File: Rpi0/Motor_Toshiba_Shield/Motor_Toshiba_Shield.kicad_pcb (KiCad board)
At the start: 2 copper layers, 29.8 x 64.8 mm, 34 parts, among them J1 Screw_Terminal_01x02, J10 Conn_01x04_Female, J11 Conn_01x04_Female, J2 Conn_02x01, J3 Screw_Terminal_01x02, J4 Screw_Terminal_01x02, J5 Screw_Terminal_01x02, J6 Screw_Terminal_01x02, J7 Conn_02x01, J8 Conn_01x04_Female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

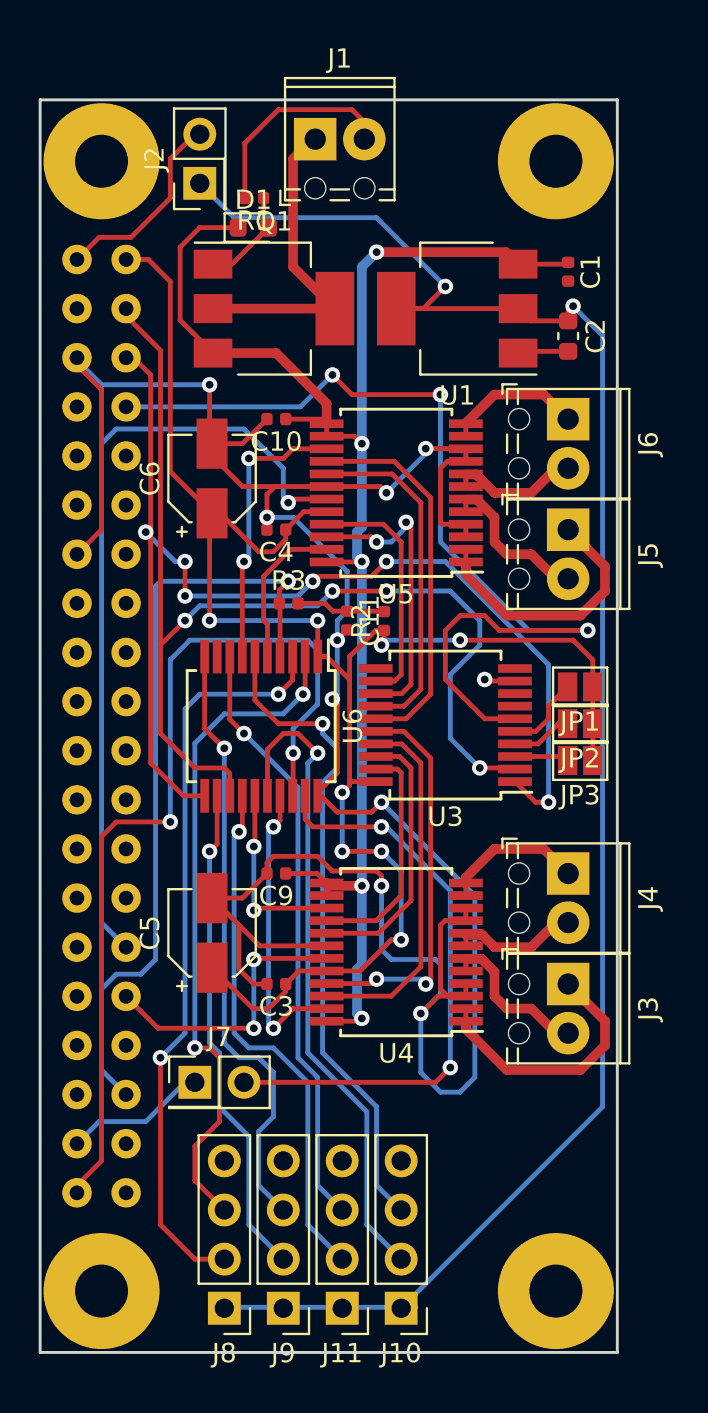
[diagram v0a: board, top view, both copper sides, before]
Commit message: Fixed rpi0 connector
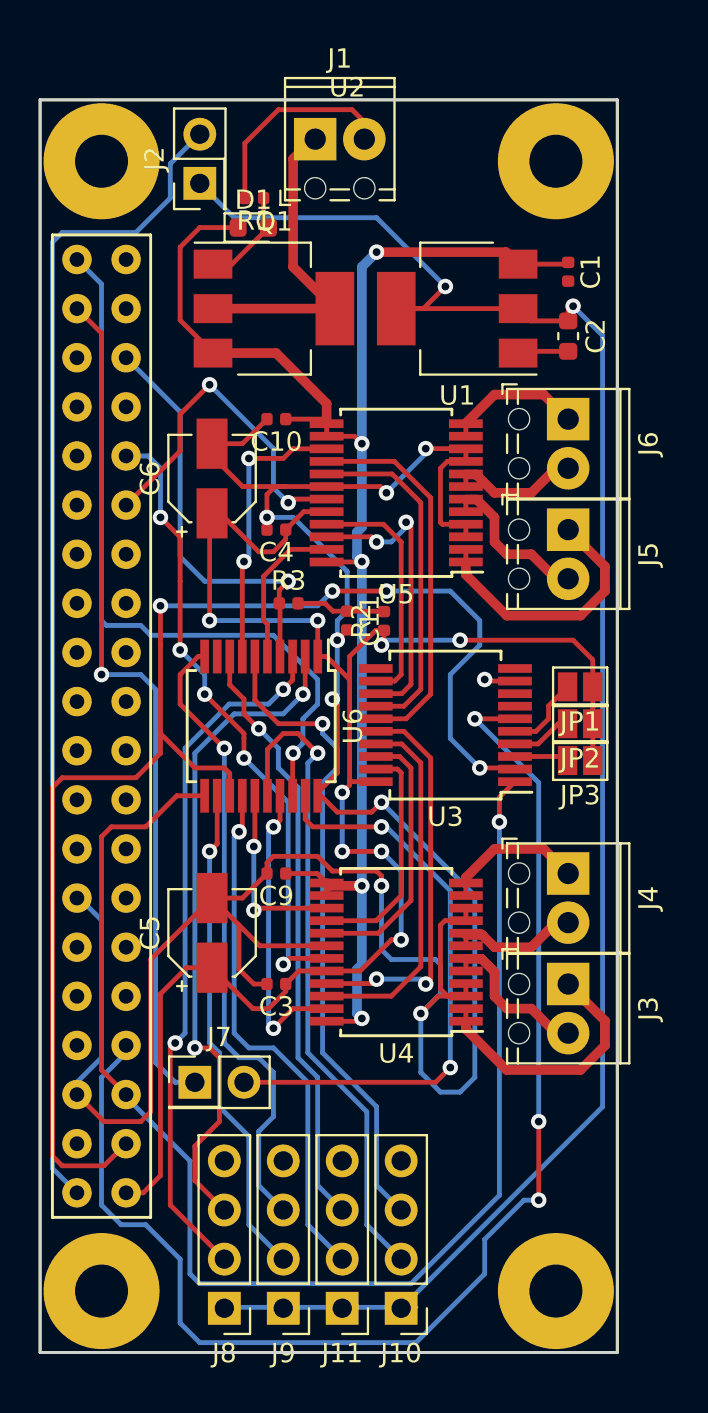
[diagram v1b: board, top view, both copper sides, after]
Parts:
- U2: moved to F.Cu
- moved U2 5.08 mm to (117.5, 97.2)
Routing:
- net Net-(J2-Pad2): track 10.2 -> 61.3 mm
- net ICSP_DAT: track 7.41 -> 44.3 mm, vias 0 -> 1
- net EN1: track 41.1 -> 17.9 mm, vias 1 -> 2
- net RES: track 49.5 -> 68.7 mm
- net EN2: track 14.6 -> 32.9 mm, vias 2 -> 5
- net MCLR: track 39.8 -> 21.7 mm
- net SDA: track 57.3 -> 71.3 mm
- net ICSP_CLK: track 48.2 -> 38.2 mm, vias 2 -> 1
- net SCL: track 61.3 -> 70.5 mm, vias 6 -> 1
- net BAT-: track 153.5 -> 159.9 mm, vias 10 -> 9
- net A1: track 38.6 -> 36.1 mm
- net B2: track 31.5 -> 32.8 mm
- net +3V3: track 89.5 -> 88.7 mm
